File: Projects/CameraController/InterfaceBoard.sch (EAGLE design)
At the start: 17 parts, among them J1 TLW-104-05-G-S, J2 TLW-104-05-G-S, J3 TLW-104-05-G-S, J4 TLW-104-05-G-S, J5 TS-103-G-A, J6 TS-103-G-A, J7 TS-103-G-A, Q1 2N7000, Q2 2N7000

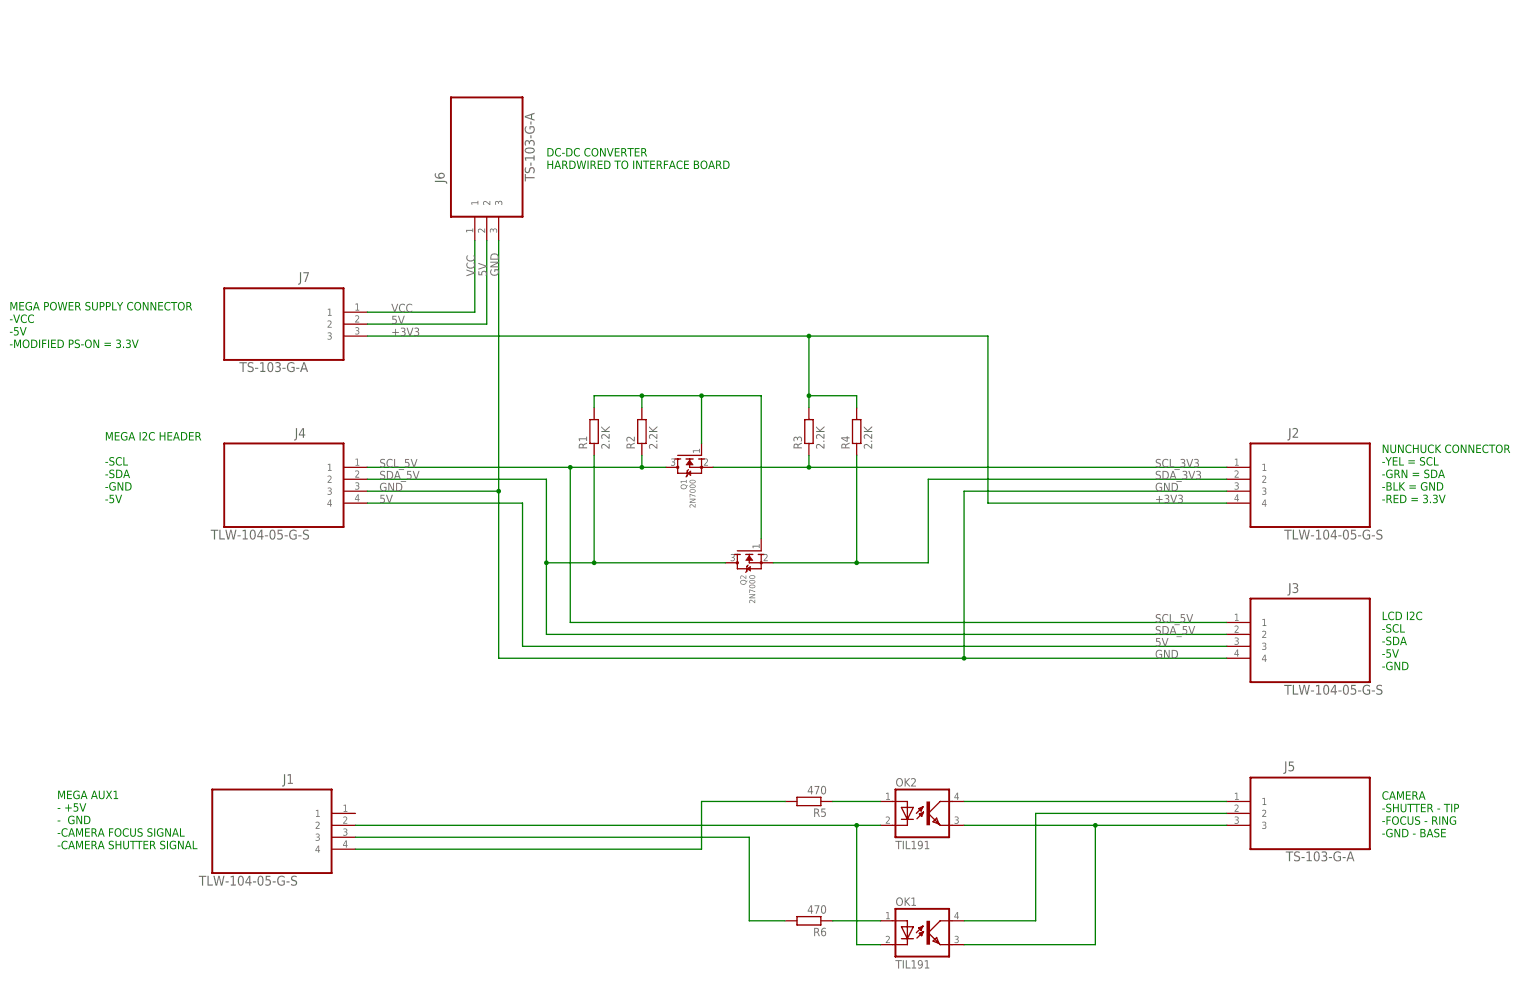
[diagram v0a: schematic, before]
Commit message: Update Camera Controller Interface PCB
Also fixed the 2N7000 part in the Adafruit library to correct the pinout
for a thru-hole part.
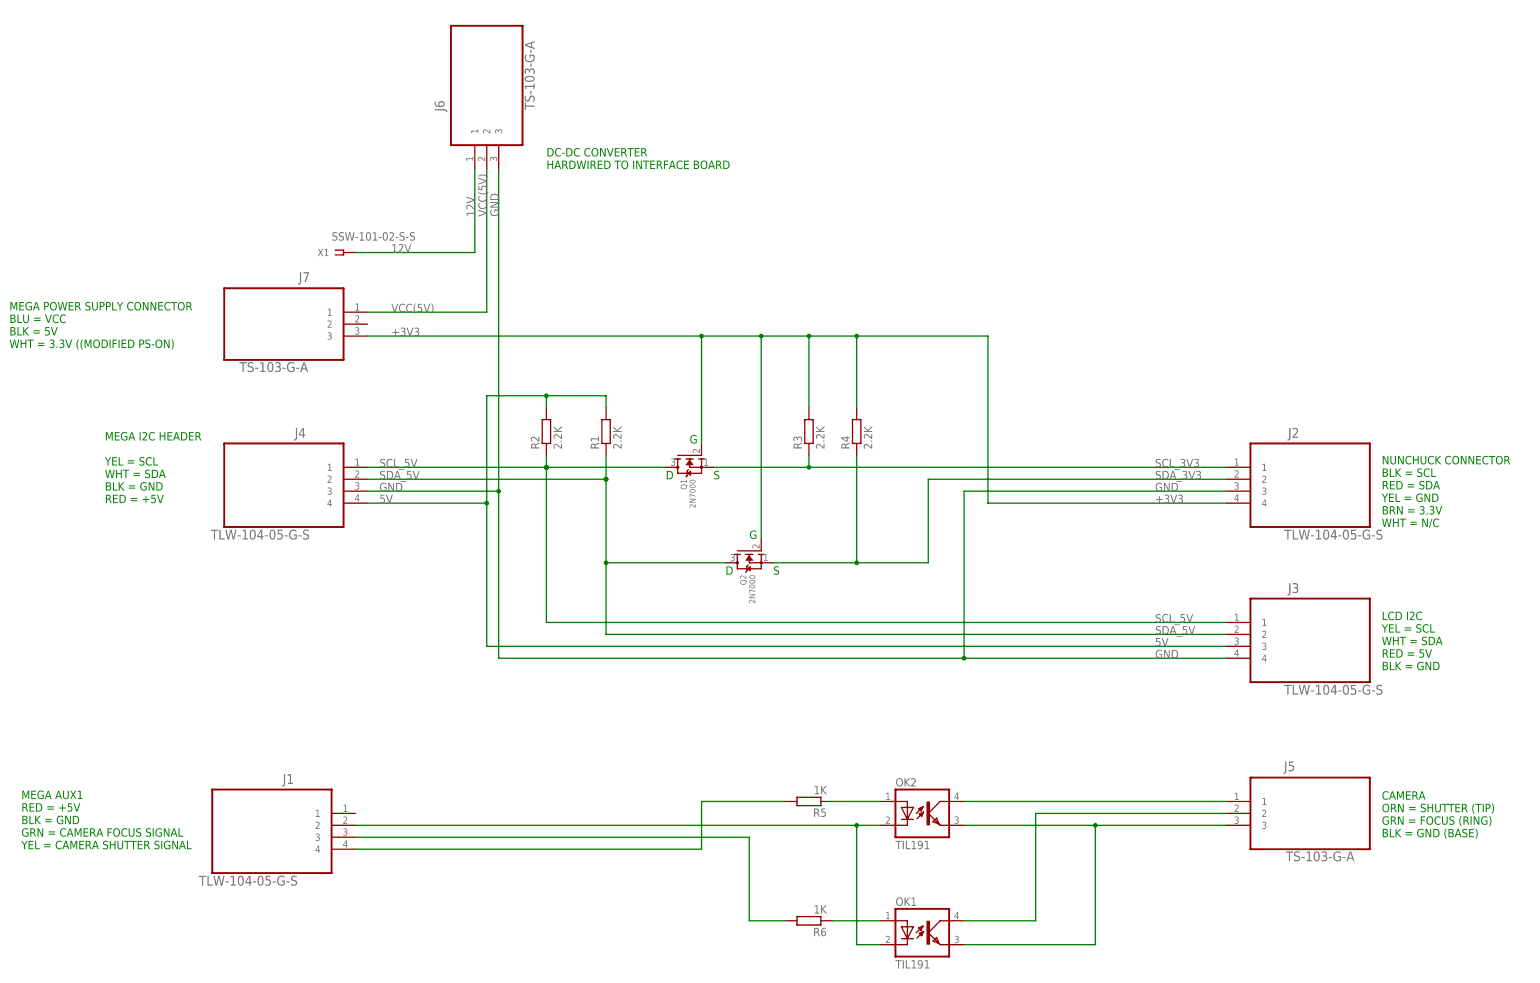
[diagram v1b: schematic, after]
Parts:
- added X1: SSW-101-02-S-S, con-samtec:SSW-101-02-S-S
- R5, R6: value 470 -> 1K
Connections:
- removed net VCC: J6.1, J7.1
- new net 12V: J6.1, X1.1
- new net VCC(5V): J6.2, J7.1
- net +3V3: no longer R1.2, R2.2
- net 5V: now also R1.2, R2.2; no longer J6.2, J7.2
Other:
- note added: "CAMERA ORN = SHUTTER (TIP) GRN = FOCUS (RING) BLK = GND (BASE)"
- note added: "D"
- note added: "G"
- note added: "LCD I2C YEL = SCL WHT = SDA RED = 5V BLK = GND"
- note added: "MEGA AUX1 RED = +5V BLK = GND GRN = CAMERA FOCUS SIGNAL YEL = CAMERA SHUTTER SIGNAL"
- note added: "MEGA I2C HEADER YEL = SCL WHT = SDA BLK = GND RED = +5V"
- note added: "MEGA POWER SUPPLY CONNECTOR BLU = VCC BLK = 5V WHT = 3.3V ((MODIFIED PS-ON)"
- note added: "NUNCHUCK CONNECTOR BLK = SCL RED = SDA YEL = GND BRN = 3.3V WHT = N/C"
- note added: "S"
- note removed: "CAMERA -SHUTTER - TIP -FOCUS - RING -GND - BASE"
- note removed: "LCD I2C -SCL -SDA -5V -GND"
- note removed: "MEGA AUX1 - +5V - GND -CAMERA FOCUS SIGNAL -CAMERA SHUTTER SIGNAL"
- note removed: "MEGA I2C HEADER -SCL -SDA -GND -5V"
- note removed: "MEGA POWER SUPPLY CONNECTOR -VCC -5V -MODIFIED PS-ON = 3.3V"
- note removed: "NUNCHUCK CONNECTOR -YEL = SCL -GRN = SDA -BLK = GND -RED = 3.3V"
- moved on the sheet: J6, R1, R2
